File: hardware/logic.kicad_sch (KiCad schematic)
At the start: 59 parts, among them J1 Hanrun HY931147C, SW1 SW_Push, U2 KSZ8851SNL, U3 SRV05-4, U4 ESP32-C3-WROOM-02, U5 AMS1117-3.3, Y1 25MHz

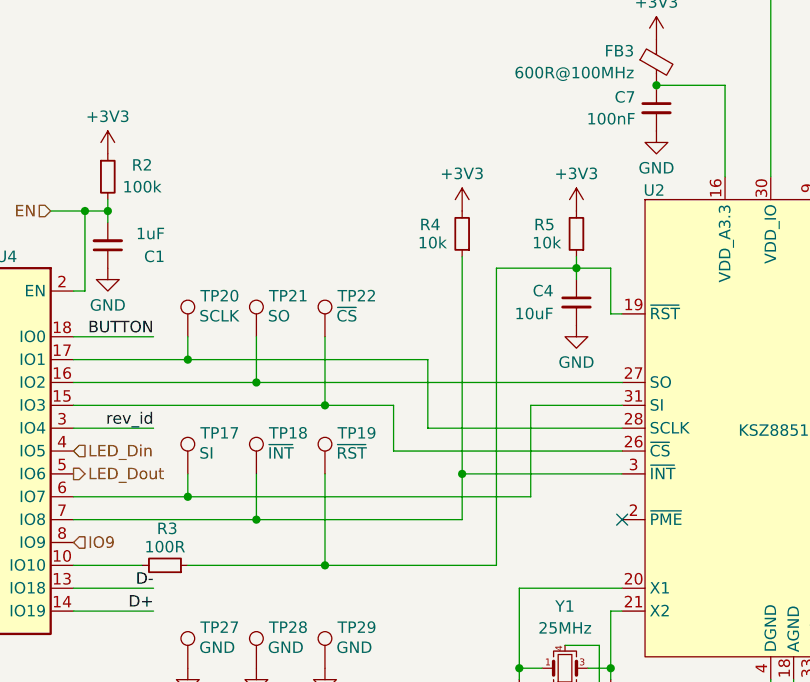
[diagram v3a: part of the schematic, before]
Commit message: hardware: pull up GPIO2
There is a bit of an ominous sentence in the ESP32-C3 datasheet:
"GPIO2 actually does not determine SPI Boot and Joint Download Boot mode,
but it is recommended to pull this pin up due to glitches."

Switch GPIO2 to an input pin on the KSZ8851 and pull it up to VDD to avoid
any possible issues.
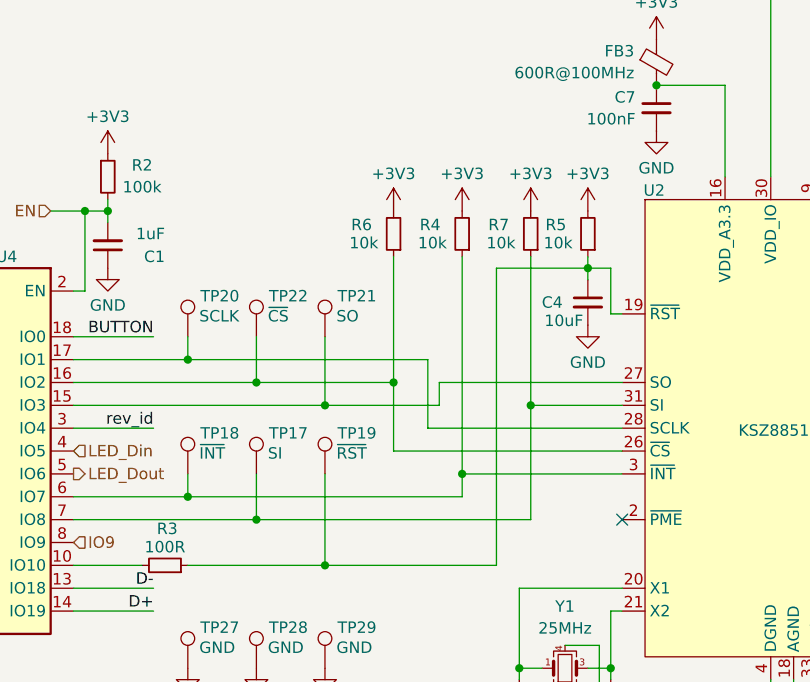
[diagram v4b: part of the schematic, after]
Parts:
- added R6, R7: 10k, Resistor_SMD:R_0402_1005Metric, symbol Device:R_Small
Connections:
- net +3V3: now also R6.2, R7.2
- net at TP21.1, U2.27 (SO): now also U4.15 (IO3); no longer U4.16 (IO2)
- net at R4.1, TP18.1, U2.3 (~{INT}): now also U4.6 (IO7); no longer U4.7 (IO8)
- net at TP22.1, U2.26 (~{CS}): now also U4.16 (IO2), R6.1; no longer U4.15 (IO3)
- net at TP17.1, U2.31 (SI): now also U4.7 (IO8), R7.1; no longer U4.6 (IO7)
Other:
- moved on the sheet: C4, R5, TP17, TP18, TP21, TP22

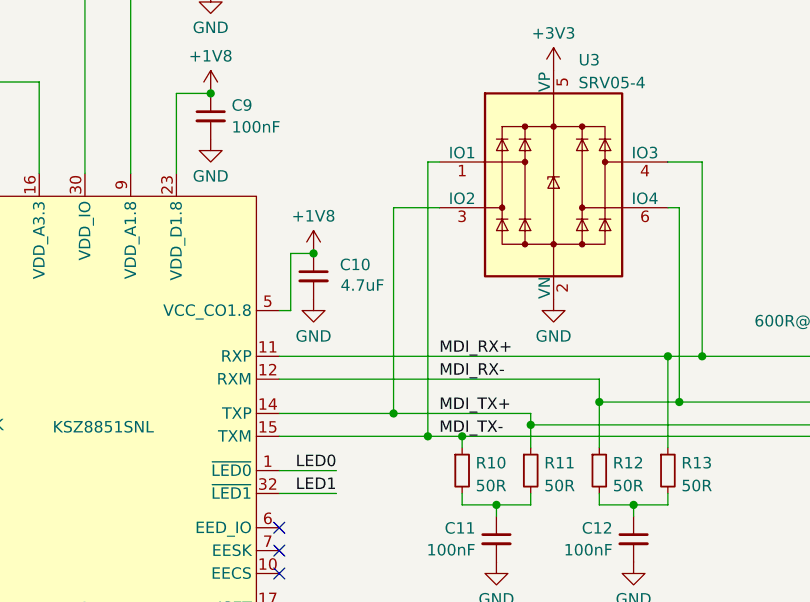
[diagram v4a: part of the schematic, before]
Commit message: hardware: add LCSC partnumber to ESP32-C3 module
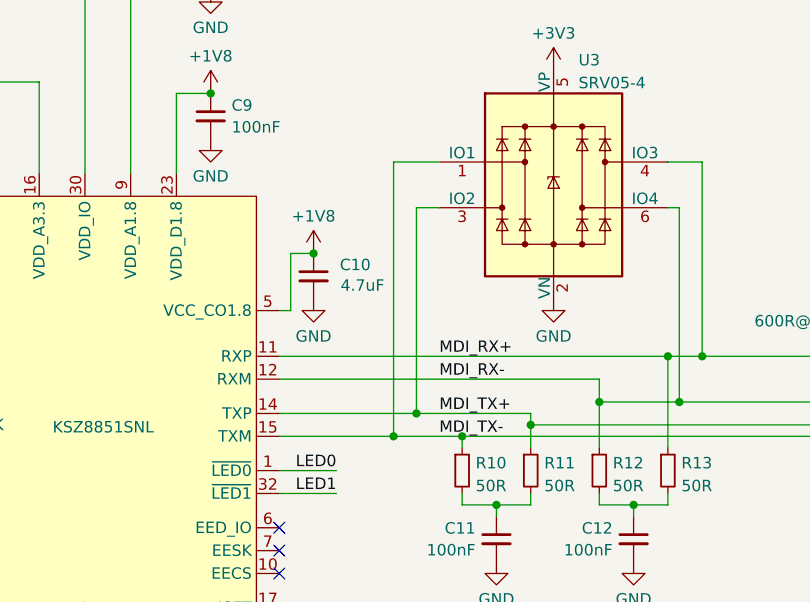
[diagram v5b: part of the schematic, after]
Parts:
- U4: LCSC (none) -> C2934560
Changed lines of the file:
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@@
 	)
 	(junction
+		(at 167.64 123.19)
+		(diameter 0)
+		(color 0 0 0 0)
+	)
+	(junction
 		(at 106.68 119.38)
 		(diameter 0)
@@
 	)
 	(junction
-		(at 171.45 123.19)
-		(diameter 0)
-		(color 0 0 0 0)
-	)
-	(junction
 		(at 76.2 116.84)
 		(diameter 0)
@@
 	)
 	(junction
-		(at 120.65 83.82)
+		(at 170.18 120.65)
 		(diameter 0)
 		(color 0 0 0 0)
 	)
 	(junction
-		(at 167.64 120.65)
+		(at 120.65 83.82)
 		(diameter 0)
 		(color 0 0 0 0)
@@
 	(wire
 		(pts
-			(xy 171.45 92.71) (xy 171.45 123.19)
-		)
-		(stroke
-			(width 0)
-			(type default)
-		)
-	)
-	(wire
-		(pts
 			(xy 96.52 119.38) (xy 96.52 116.84)
 		)
@@
 	(wire
 		(pts
-			(xy 154.94 123.19) (xy 171.45 123.19)
+			(xy 154.94 123.19) (xy 167.64 123.19)
 		)
 		(stroke
@@
 	(wire
 		(pts
-			(xy 172.72 92.71) (xy 171.45 92.71)
-		)
-		(stroke
-			(width 0)
-			(type default)
-		)
-	)
-	(wire
-		(pts
 			(xy 40.64 101.6) (xy 40.64 99.06)
 		)
@@
 	(wire
 		(pts
-			(xy 167.64 97.79) (xy 167.64 120.65)
-		)
-		(stroke
-			(width 0)
-			(type default)
-		)
-	)
-	(wire
-		(pts
 			(xy 190.5 116.84) (xy 190.5 119.38)
 		)
@@
 	(wire
 		(pts
+			(xy 167.64 92.71) (xy 172.72 92.71)
+		)
+		(stroke
+			(width 0)
+			(type default)
+		)
+	)
+	(wire
+		(pts
 			(xy 64.77 121.92) (xy 55.88 121.92)
 		)
@@
 	(wire
 		(pts
-			(xy 171.45 123.19) (xy 175.26 123.19)
+			(xy 167.64 123.19) (xy 175.26 123.19)
 		)
 		(stroke
@@
 	(wire
 		(pts
+			(xy 172.72 97.79) (xy 170.18 97.79)
+		)
+		(stroke
+			(width 0)
+			(type default)
+		)
+	)
+	(wire
+		(pts
 			(xy 55.88 119.38) (xy 83.82 119.38)
 		)
@@
 	(wire
 		(pts
+			(xy 170.18 97.79) (xy 170.18 120.65)
+		)
+		(stroke
+			(width 0)
+			(type default)
+		)
+	)
+	(wire
+		(pts
 			(xy 175.26 130.81) (xy 179.07 130.81)
 		)
@@
 	(wire
 		(pts
+			(xy 167.64 92.71) (xy 167.64 123.19)
+		)
+		(stroke
+			(width 0)
+			(type default)
+		)
+	)
+	(wire
+		(pts
 			(xy 22.86 106.68) (xy 25.4 106.68)
 		)
@@
 	(wire
 		(pts
-			(xy 167.64 120.65) (xy 182.88 120.65)
+			(xy 119.38 62.23) (xy 129.54 62.23)
 		)
 		(stroke
@@
 	(wire
 		(pts
-			(xy 119.38 62.23) (xy 129.54 62.23)
+			(xy 170.18 120.65) (xy 182.88 120.65)
 		)
 		(stroke
@@
 	(wire
 		(pts
-			(xy 154.94 120.65) (xy 167.64 120.65)
+			(xy 154.94 120.65) (xy 170.18 120.65)
 		)
 		(stroke
@@
 	(wire
 		(pts
-			(xy 167.64 97.79) (xy 172.72 97.79)
-		)
-		(stroke
-			(width 0)
-			(type default)
-		)
-	)
-	(wire
-		(pts
 			(xy 254 151.13) (xy 243.84 151.13)
 		)
@@
 			(effects
 				(font
+					(size 1.27 1.27)
+				)
+				(hide yes)
+			)
+		)
+		(property "LCSC" "C2934560"
+			(at 40.64 124.46 0)
+			(effects
+				(font

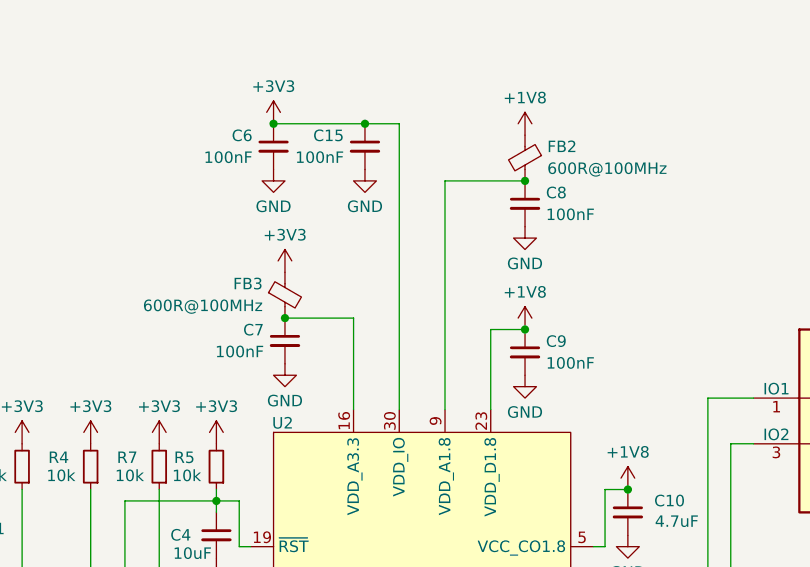
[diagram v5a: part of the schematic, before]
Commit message: hardware: upgrade decoupling caps on ferrite beads to 1µF
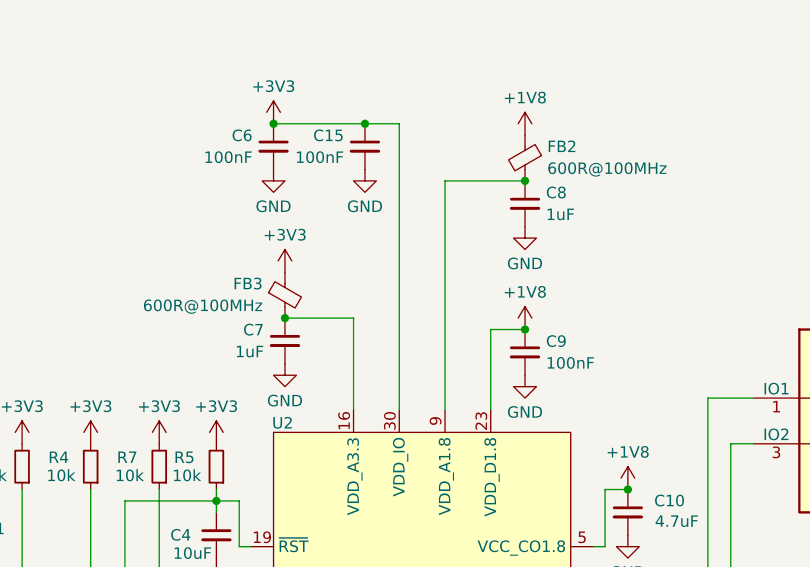
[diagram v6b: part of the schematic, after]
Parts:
- C7, C8: value 100nF -> 1uF; LCSC C1525 -> C52923
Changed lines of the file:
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@@
 			)
 		)
-		(property "Value" "100nF"
+		(property "Value" "1uF"
 			(at 149.6441 72.3384 0)
 			(effects
@@
 			)
 		)
-		(property "LCSC" "C1525"
+		(property "LCSC" "C52923"
 			(at 147.32 71.12 0)
 			(effects
@@
 			)
 		)
-		(property "Value" "100nF"
+		(property "Value" "1uF"
 			(at 118.3259 87.5784 0)
 			(effects
@@
 			)
 		)
-		(property "LCSC" "C1525"
+		(property "LCSC" "C52923"
 			(at 120.65 86.36 0)
 			(effects

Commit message: Implement review comments by Urmel
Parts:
- added C22, C23: 100nF, Capacitor_SMD:C_0402_1005Metric, symbol Device:C_Small
- added R16: 100R, Resistor_SMD:R_0402_1005Metric, symbol Device:R_Small
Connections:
- net +3V3: now also C22.1, C23.1
- net AGND: now also C22.2, C23.2
- net BUTTON: now also R16.2; no longer R28.2, SW1.1
- new net: R16.1, R28.2, SW1.1

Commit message: Exclude parts with virtual footprints from BOM
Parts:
- R50: LCSC C25744 -> (none)
- TP15, TP16, TP17, TP18, TP19, TP20, TP21, TP22, TP27, TP28, TP29, TP30, TP31, TP32: now left out of the parts list
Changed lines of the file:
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@@
 		(unit 1)
 		(exclude_from_sim no)
-		(in_bom yes)
+		(in_bom no)
 		(on_board yes)
 		(dnp no)
@@
 		(unit 1)
 		(exclude_from_sim no)
-		(in_bom yes)
+		(in_bom no)
 		(on_board yes)
 		(dnp no)
@@
 		(unit 1)
 		(exclude_from_sim no)
-		(in_bom yes)
+		(in_bom no)
 		(on_board yes)
 		(dnp no)
@@
 		(unit 1)
 		(exclude_from_sim no)
-		(in_bom yes)
+		(in_bom no)
 		(on_board yes)
 		(dnp no)
@@
 		(unit 1)
 		(exclude_from_sim no)
-		(in_bom yes)
+		(in_bom no)
 		(on_board yes)
 		(dnp no)
@@
 		(unit 1)
 		(exclude_from_sim no)
-		(in_bom yes)
+		(in_bom no)
 		(on_board yes)
 		(dnp no)
@@
 		(unit 1)
 		(exclude_from_sim no)
-		(in_bom yes)
+		(in_bom no)
 		(on_board yes)
 		(dnp no)
@@
 		(unit 1)
 		(exclude_from_sim no)
-		(in_bom yes)
+		(in_bom no)
 		(on_board yes)
 		(dnp no)
@@
 		(unit 1)
 		(exclude_from_sim no)
-		(in_bom yes)
+		(in_bom no)
 		(on_board yes)
 		(dnp no)
@@
 		(unit 1)
 		(exclude_from_sim no)
-		(in_bom yes)
+		(in_bom no)
 		(on_board yes)
 		(dnp no)
@@
 		(unit 1)
 		(exclude_from_sim no)
-		(in_bom yes)
+		(in_bom no)
 		(on_board yes)
 		(dnp no)
@@
 			)
 		)
-		(property "LCSC" "C25744"
-			(at 86.36 163.83 0)
-			(effects
-				(font
-					(size 1.27 1.27)
-				)
-				(hide yes)
-			)
-		)
 		(pin "1"
 		)
@@
 		(unit 1)
 		(exclude_from_sim no)
-		(in_bom yes)
+		(in_bom no)
 		(on_board yes)
 		(dnp no)
@@
 		(unit 1)
 		(exclude_from_sim no)
-		(in_bom yes)
+		(in_bom no)
 		(on_board yes)
 		(dnp no)
@@
 		(unit 1)
 		(exclude_from_sim no)
-		(in_bom yes)
+		(in_bom no)
 		(on_board yes)
 		(dnp no)
